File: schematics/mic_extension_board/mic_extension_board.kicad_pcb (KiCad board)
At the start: 2 copper layers, 85.1 x 62.2 mm, 75 parts, among them J1 XLR3, J2 Conn_01x02_Male, J3 Aux In, J4 I2C Bus, J5 6Pin ISP, J6 Input/Output, J7 XLR3, J8 XLR3, J9 Conn_01x03_Female, SW1 Stompbutton 1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

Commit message: last changes before order
* fixed last minor details
* tidied gitignore files
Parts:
- removed C4, C6: 10uF, Capacitor_SMD:CP_Elec_4x4.5
- removed C5, C7: 22uF, Capacitor_SMD:CP_Elec_4x4.5
- added J10: Conn_01x01_Male, Connector_PinHeader_2.54mm:PinHeader_1x01_P2.54mm_Vertical, F.Cu at (61.6, 60.3)
- added TP1: TestPoint, TestPoint:TestPoint_Pad_D1.5mm, F.Cu at (53.3, 43.2)
- added TP2: TestPoint, TestPoint:TestPoint_Pad_D1.5mm, F.Cu at (45.7, 38.7)
- added TP3: TestPoint, TestPoint:TestPoint_Pad_D1.5mm, F.Cu at (50.2, 48.3)
- J5: footprint Connector_PinHeader_1.27mm:PinHeader_2x03_P1.27mm_Vertical -> Connector_PinHeader_2.54mm:PinHeader_2x03_P2.54mm_Vertical
- moved R8 2.56 mm to (66.0, 66.0)
- moved D7 2.54 mm to (66.0, 59.7)
- moved U3 1.42 mm to (61.6, 65.4)
- moved D5 1.27 mm to (69.8, 59.7)
- moved R7 1.27 mm to (69.8, 66.3)
- turned C13 to 180 degrees
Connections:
- C13 pad 1: -9V -> GND
- C13 pad 2: GND -> -9V
- J3 pad 1: Net-(C5-Pad2) -> Net-(J3-Pad1)
- J3 pad 2: Net-(C7-Pad2) -> Net-(J3-Pad2)
- J6 pad 3: Net-(C6-Pad2) -> Net-(J6-Pad3)
- J6 pad 4: Net-(C4-Pad2) -> Net-(J6-Pad4)
- R19 pad 1: Net-(C4-Pad1) -> Net-(J6-Pad4)
- R20 pad 1: Net-(C5-Pad1) -> Net-(J3-Pad1)
- R22 pad 1: Net-(C6-Pad1) -> Net-(J6-Pad3)
- R23 pad 1: Net-(C7-Pad1) -> Net-(J3-Pad2)
- U3 pad 3: +9V -> Net-(U3-Pad3)
- U4 pad 1: unconnected-(U4-Pad1) -> Net-(TP2-Pad1)
- U4 pad 5: unconnected-(U4-Pad5) -> Net-(TP3-Pad1)
- U4 pad 8: unconnected-(U4-Pad8) -> Net-(TP1-Pad1)
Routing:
- net Net-(C5-Pad1): track 48.4 -> 0.00 mm, vias 2 -> 0
- net Net-(J3-Pad1): track 0.00 -> 46.7 mm, vias 0 -> 1
- net Net-(J6-Pad3): track 0.00 -> 15.0 mm
- net Net-(J3-Pad2): track 0.00 -> 13.8 mm
- net Net-(C4-Pad2): track 8.10 -> 0.00 mm
- net Net-(J6-Pad4): track 0.00 -> 8.01 mm
- net Net-(C6-Pad1): track 7.38 -> 0.00 mm
- net Net-(C7-Pad2): track 6.61 -> 0.00 mm
- net Net-(C6-Pad2): track 5.37 -> 0.00 mm
- net Net-(C5-Pad2): track 4.97 -> 0.00 mm
- net Net-(J6-Pad1): track 55.6 -> 50.7 mm
- net Net-(U3-Pad3): track 0.00 -> 4.14 mm
- net Net-(C4-Pad1): track 3.95 -> 0.00 mm
- net Net-(TP1-Pad1): track 0.00 -> 3.35 mm
- net Net-(TP2-Pad1): track 0.00 -> 3.33 mm
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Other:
- board text added: "AC In"
- board text added: "AdcIn"
- board text added: "AuxIn"
- board text added: "DacL"
- board text added: "DacR"
- board text added: "I2C"
- board text added: "ISP"
- board text added: "MicIn"
- board text added: "OutL"
- board text added: "OutR"
- board text added: "Phones"
- board text added: "Vol."

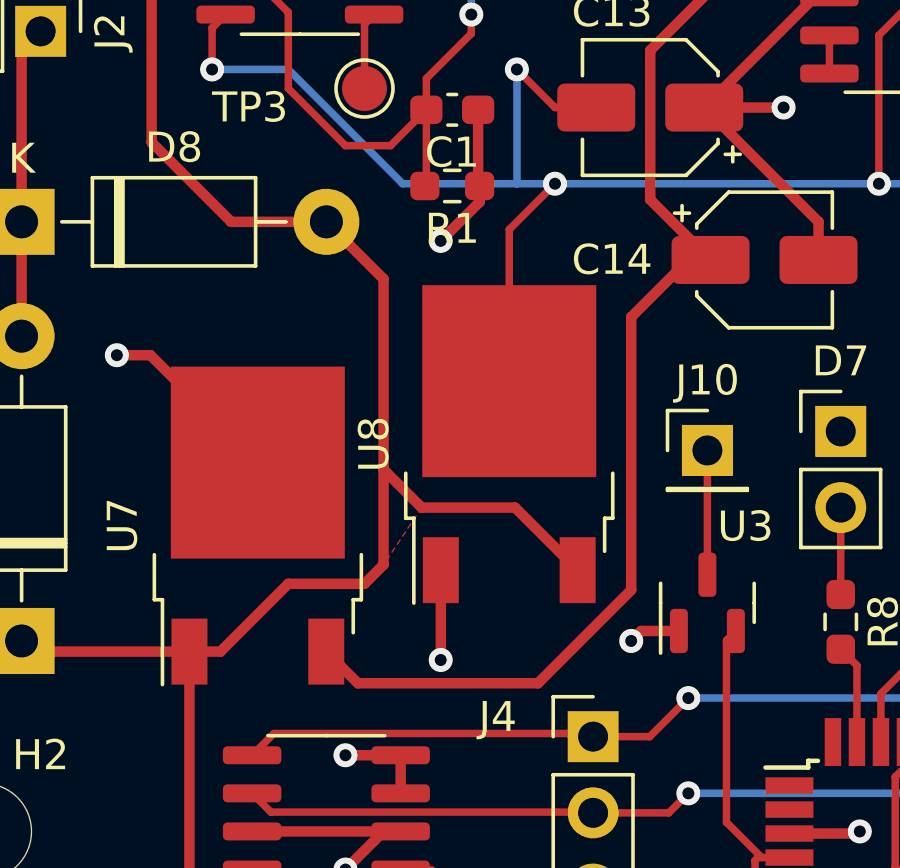
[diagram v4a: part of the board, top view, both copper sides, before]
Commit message: expansio board firmware
* added settings for avr gcc
* fixed minor bug
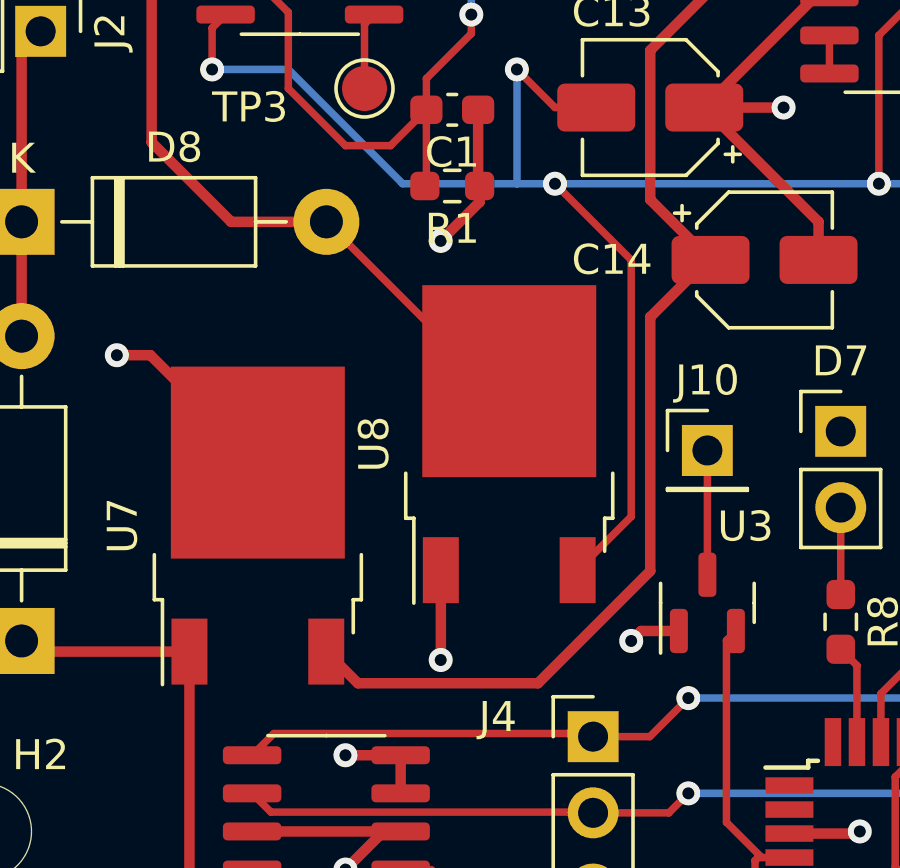
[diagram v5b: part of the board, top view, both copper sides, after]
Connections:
- C2 pad 1: +12V -> Net-(C2-Pad1)
- C3 pad 2: +12V -> Net-(D8-Pad2)
- D1 pad 1: +12V -> Net-(C2-Pad1)
- D8 pad 2: +12V -> Net-(D8-Pad2)
- U7 pad 1: +12V -> Net-(C2-Pad1)
- U8 pad 2: -9V -> Net-(D8-Pad2)
- U8 pad 3: +12V -> -9V
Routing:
- net +12V: track 62.6 -> 0.00 mm
- net Net-(D8-Pad2): track 0.00 -> 26.7 mm
- net Net-(C2-Pad1): track 0.00 -> 16.0 mm
- net -9V: track 81.1 -> 88.6 mm
- removed copper zone on F.Cu, net +12V

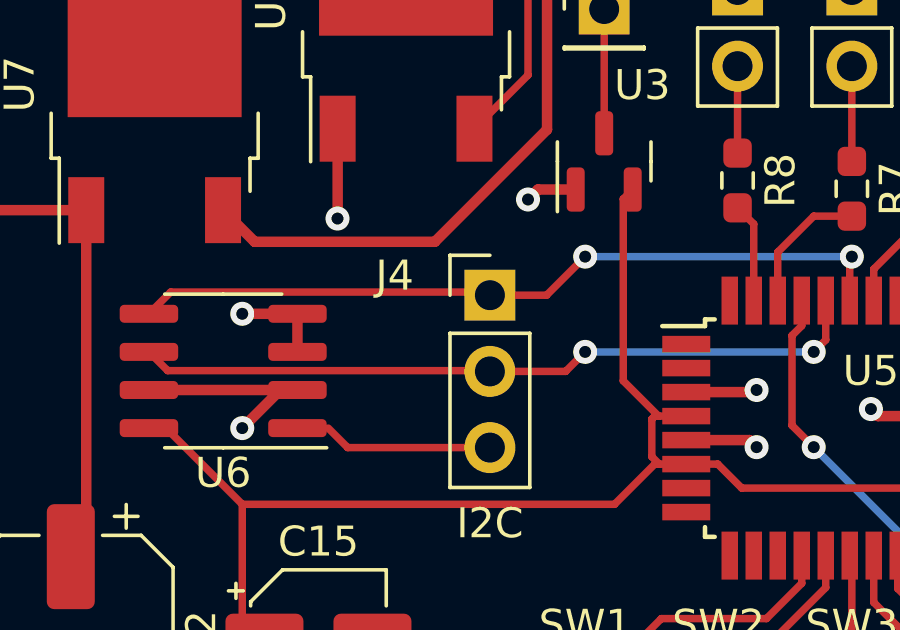
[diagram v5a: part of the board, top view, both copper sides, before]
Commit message: schematic: changed some footprints & fixed errors
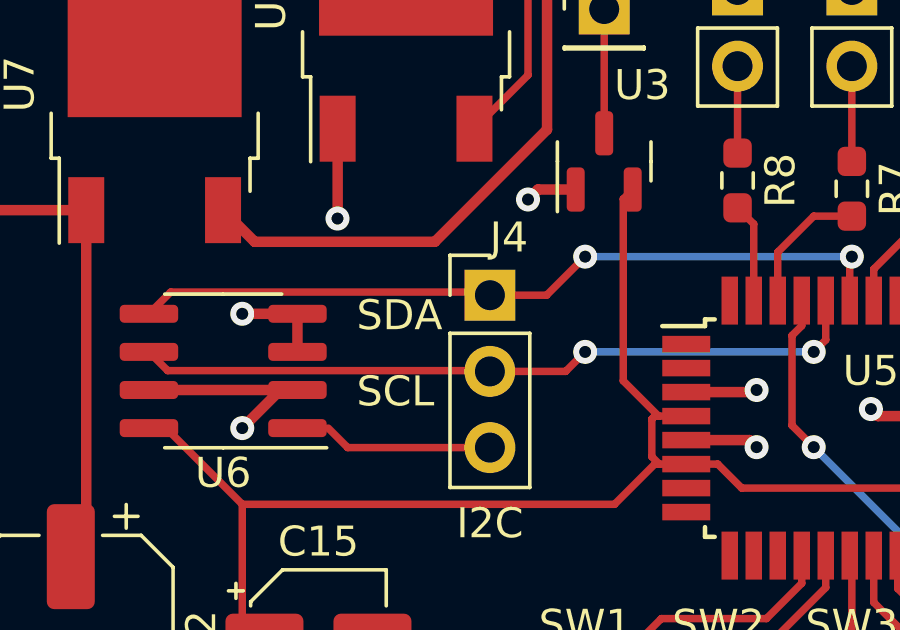
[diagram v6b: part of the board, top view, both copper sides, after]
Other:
- board text added: "SCL"
- board text added: "SDA"

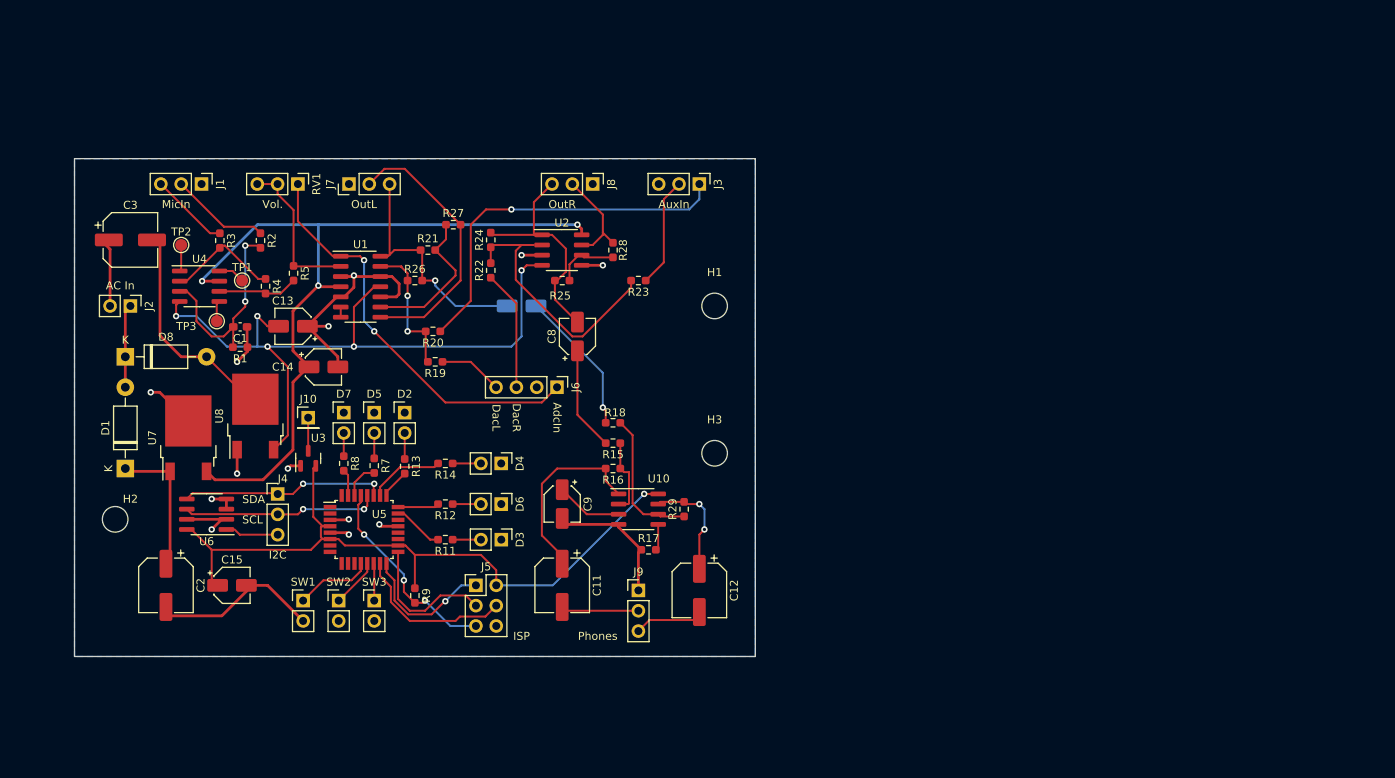
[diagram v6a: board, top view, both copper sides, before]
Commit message: modified extension board schematic
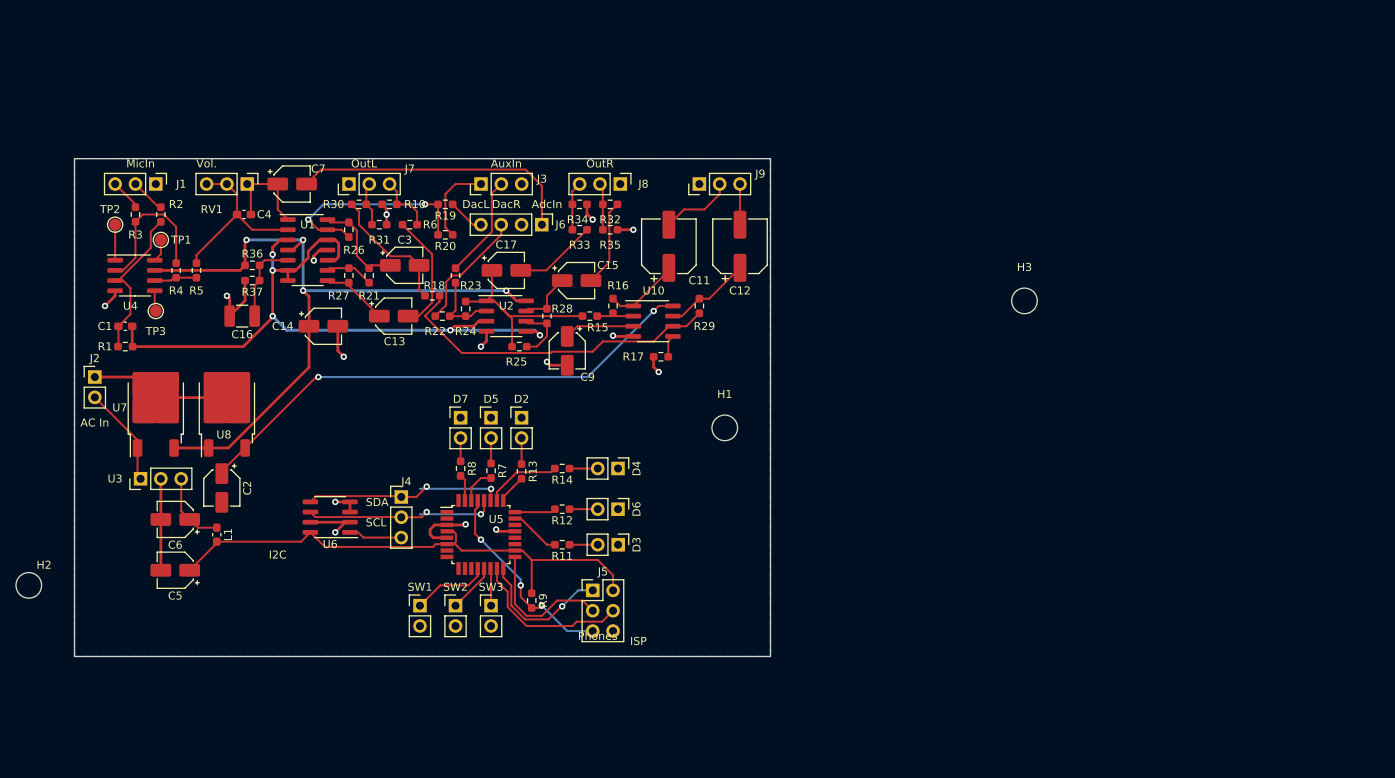
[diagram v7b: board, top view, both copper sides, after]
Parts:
- removed C10, C8: 0.33uF, Capacitor_SMD:CP_Elec_4x4.5
- removed D1, D8: 1N4001, Diode_THT:D_DO-41_SOD81_P10.16mm_Horizontal
- removed J10: Conn_01x01_Male, Connector_PinHeader_2.54mm:PinHeader_1x01_P2.54mm_Vertical
- added C16: 0.1uF, Capacitor_SMD:C_1210_3225Metric_Pad1.33x2.70mm_HandSolder, F.Cu at (53.3, 47.6)
- added C17: 10uF, Capacitor_SMD:CP_Elec_4x4.5, F.Cu at (86.4, 41.9)
- added C4: 47pF, Capacitor_SMD:C_0603_1608Metric_Pad1.08x0.95mm_HandSolder, F.Cu at (53.6, 34.9)
- added C5: 22uF, Capacitor_SMD:CP_Elec_4x4.5, F.Cu at (45.0, 79.4)
- added C6: 22uF, Capacitor_SMD:CP_Elec_4x4.5, F.Cu at (45.0, 73.0)
- added C7: 1uF, Capacitor_SMD:CP_Elec_4x4.5, F.Cu at (59.6, 31.1)
- added L1: 22uH, Inductor_SMD:L_0603_1608Metric_Pad1.05x0.95mm_HandSolder, F.Cu at (50.2, 74.9)
- added R10: 10k, Resistor_SMD:R_0603_1608Metric_Pad0.98x0.95mm_HandSolder, F.Cu at (71.8, 33.7)
- added R30: 150, Resistor_SMD:R_0603_1608Metric_Pad0.98x0.95mm_HandSolder, F.Cu at (67.9, 33.7)
- added R31: 10k, Resistor_SMD:R_0603_1608Metric_Pad0.98x0.95mm_HandSolder, F.Cu at (70.5, 36.2)
- added R32: 150, Resistor_SMD:R_0603_1608Metric_Pad0.98x0.95mm_HandSolder, F.Cu at (99.3, 33.7)
- added R33: 150, Resistor_SMD:R_0603_1608Metric_Pad0.98x0.95mm_HandSolder, F.Cu at (95.5, 36.8)
- added R34: 10k, Resistor_SMD:R_0603_1608Metric_Pad0.98x0.95mm_HandSolder, F.Cu at (95.5, 33.7)
- added R35: 10k, Resistor_SMD:R_0603_1608Metric_Pad0.98x0.95mm_HandSolder, F.Cu at (99.3, 36.8)
- added R36: 12k, Resistor_SMD:R_0603_1608Metric_Pad0.98x0.95mm_HandSolder, F.Cu at (54.6, 41.3)
- added R37: 12k, Resistor_SMD:R_0603_1608Metric_Pad0.98x0.95mm_HandSolder, F.Cu at (54.6, 43.2)
- added R6: 150, Resistor_SMD:R_0603_1608Metric_Pad0.98x0.95mm_HandSolder, F.Cu at (74.3, 36.2)
- C13: value 22uF -> 10uF
- C15: value 2.2uF -> 10uF
- C2: value 220uF -> 1uF; footprint Capacitor_SMD:CP_Elec_6.3x7.7 -> Capacitor_SMD:CP_Elec_4x4.5
- C3: value 220uF -> 10uF; footprint Capacitor_SMD:CP_Elec_6.3x7.7 -> Capacitor_SMD:CP_Elec_4x4.5
- U3: value APE8865N-33-HF-3 -> k7833; footprint Package_TO_SOT_SMD:SOT-23 -> Connector_PinHeader_2.54mm:PinHeader_1x03_P2.54mm_Vertical
- U7: value MC78M05_TO252 -> MC78M09_TO252
- U8: value MC79M08_TO252 -> MC78M05_TO252
- moved C15 57.5 mm to (95.1, 43.2)
- moved J9 51.4 mm to (110.5, 31.1), turned to 90 degrees
- moved C11 44.4 mm to (106.7, 38.9), turned to 90 degrees
- moved C12 43.3 mm to (115.6, 38.9), turned to 90 degrees
- moved H3 43.2 mm to (151.1, 45.7)
- moved C3 34.4 mm to (73.7, 41.3)
- moved R18 27.6 mm to (77.1, 45.1)
- moved J3 27.3 mm to (83.2, 31.1), turned to 90 degrees
- moved R29 25.5 mm to (110.5, 46.4)
- moved R17 24.2 mm to (105.7, 52.7)
- moved U10 23.6 mm to (104.7, 48.3)
- moved R23 22.9 mm to (80.0, 42.5), turned to -90 degrees
- moved U3 21.1 mm to (40.6, 68.0)
- moved J6 20.4 mm to (90.8, 36.2)
- moved R16 20.3 mm to (99.7, 46.4), turned to 90 degrees
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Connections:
- C1 pad 1: GND -> VGND
- C13 pad 1: GND -> Net-(C13-Pad1)
- C13 pad 2: -9V -> Net-(C13-Pad2)
- C15 pad 2: GND -> Net-(C15-Pad2)
- C2 pad 1: Net-(C2-Pad1) -> 5V
- C3 pad 1: GND -> Net-(C3-Pad1)
- C3 pad 2: Net-(D8-Pad2) -> /Analog Preamp/Right Analog Out
- J2 pad 1: AC -> GND
- J2 pad 2: GND -> Net-(J2-Pin_2)
- J5 pad 2: Net-(C15-Pad1) -> 3V3
- J6 pad 1: Net-(J6-Pad1) -> Net-(J6-Pin_1)
- J7 pad 3: Net-(C10-Pad2) -> Net-(J7-Pad3)
- J8 pad 3: Net-(C8-Pad2) -> Net-(J8-Pad3)
- R1 pad 1: GND -> VGND
- R15 pad 2: Net-(C8-Pad1) -> /Analog Preamp/Left Analog Out
- R18 pad 2: Net-(C10-Pad1) -> /Analog Preamp/Right Analog Out
- R21 pad 1: Net-(C10-Pad2) -> Net-(C3-Pad1)
- R24 pad 2: Net-(C8-Pad2) -> /Analog Preamp/Left Analog Out
- R25 pad 1: Net-(C8-Pad2) -> /Analog Preamp/Left Analog Out
- R26 pad 2: Net-(C10-Pad2) -> Net-(C3-Pad1)
- R27 pad 2: Net-(J7-Pad2) -> Net-(C13-Pad1)
- R28 pad 2: Net-(J8-Pad2) -> Net-(C15-Pad1)
- R9 pad 1: Net-(C15-Pad1) -> 3V3
- RV1 pad 1: Net-(J6-Pad1) -> Net-(C4-Pad2)
- U1 pad 1: Net-(J6-Pad1) -> Net-(C4-Pad2)
- U1 pad 10: GND -> VGND
- U1 pad 11: -9V -> GND
- U1 pad 12: GND -> VGND
- U1 pad 14: Net-(C10-Pad2) -> Net-(C3-Pad1)
- U1 pad 3: GND -> VGND
- U1 pad 5: GND -> Net-(U1B-+)
- U1 pad 6: Net-(U1-Pad6) -> VGND
- U1 pad 7: Net-(U1-Pad6) -> VGND
- U1 pad 8: Net-(J7-Pad2) -> Net-(C13-Pad1)
- U10 pad 8: Net-(C15-Pad1) -> 5V
- U2 pad 1: Net-(C8-Pad2) -> /Analog Preamp/Left Analog Out
- U2 pad 3: GND -> VGND
- U2 pad 4: -9V -> GND
- U2 pad 5: GND -> VGND
- U2 pad 7: Net-(J8-Pad2) -> Net-(C15-Pad1)
- U3 pad 1: GND -> Net-(J2-Pin_2)
- U3 pad 2: Net-(C15-Pad1) -> GND
- U4 pad 4: -9V -> GND
- U5 pad 18: Net-(C15-Pad1) -> 3V3
- U5 pad 4: Net-(C15-Pad1) -> 3V3
- U5 pad 6: Net-(C15-Pad1) -> 3V3
- U6 pad 8: Net-(C15-Pad1) -> 3V3
- U7 pad 1: Net-(C2-Pad1) -> Net-(J2-Pin_2)
- U8 pad 1: GND -> +9V
- U8 pad 2: Net-(D8-Pad2) -> GND
- U8 pad 3: -9V -> 5V
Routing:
- net VGND: track 0.00 -> 88.9 mm, vias 0 -> 5
- net -9V: track 88.6 -> 0.00 mm, vias 5 -> 0
- net Net-(C15-Pad1): track 88.1 -> 7.04 mm, vias 1 -> 0
- net 3V3: track 0.00 -> 67.0 mm
- net 5V: track 0.00 -> 65.2 mm, vias 0 -> 2
- net Net-(J6-Pad1): track 50.7 -> 0.00 mm, vias 2 -> 0
- net Net-(J3-Pin_1): track 46.7 -> 10.4 mm, vias 1 -> 0
- net Net-(J6-Pin_1): track 0.00 -> 35.9 mm
- net GND: track 119.3 -> 89.0 mm, vias 13 -> 15
- net Net-(C10-Pad2): track 29.1 -> 0.00 mm, vias 1 -> 0
- net Net-(J7-Pad2): track 33.0 -> 5.53 mm
- net Net-(C8-Pad2): track 27.2 -> 0.00 mm
- net Net-(D8-Pad2): track 26.7 -> 0.00 mm
- net /Analog Preamp/Left Analog Out: track 0.00 -> 25.1 mm
- net Net-(U10-IN_B): track 17.8 -> 41.6 mm
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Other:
- board size 85.1 x 62.2 mm -> 87 x 62.2 mm
